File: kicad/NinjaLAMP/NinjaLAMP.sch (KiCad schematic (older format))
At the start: 33 parts, among them J1 Barrel_Jack_Switch, J2 Conn_01x05_Male, Q1 BSP89, Q2 BSP89, SW0 DIP-BUTTON_2P-6.0X3.0X4.3MM_, SW1 DIP-BUTTON_2P-6.0X3.0X4.3MM_, SW2 DIP-BUTTON_2P-6.0X3.0X4.3MM_, U1 SeeeduinoXIAO

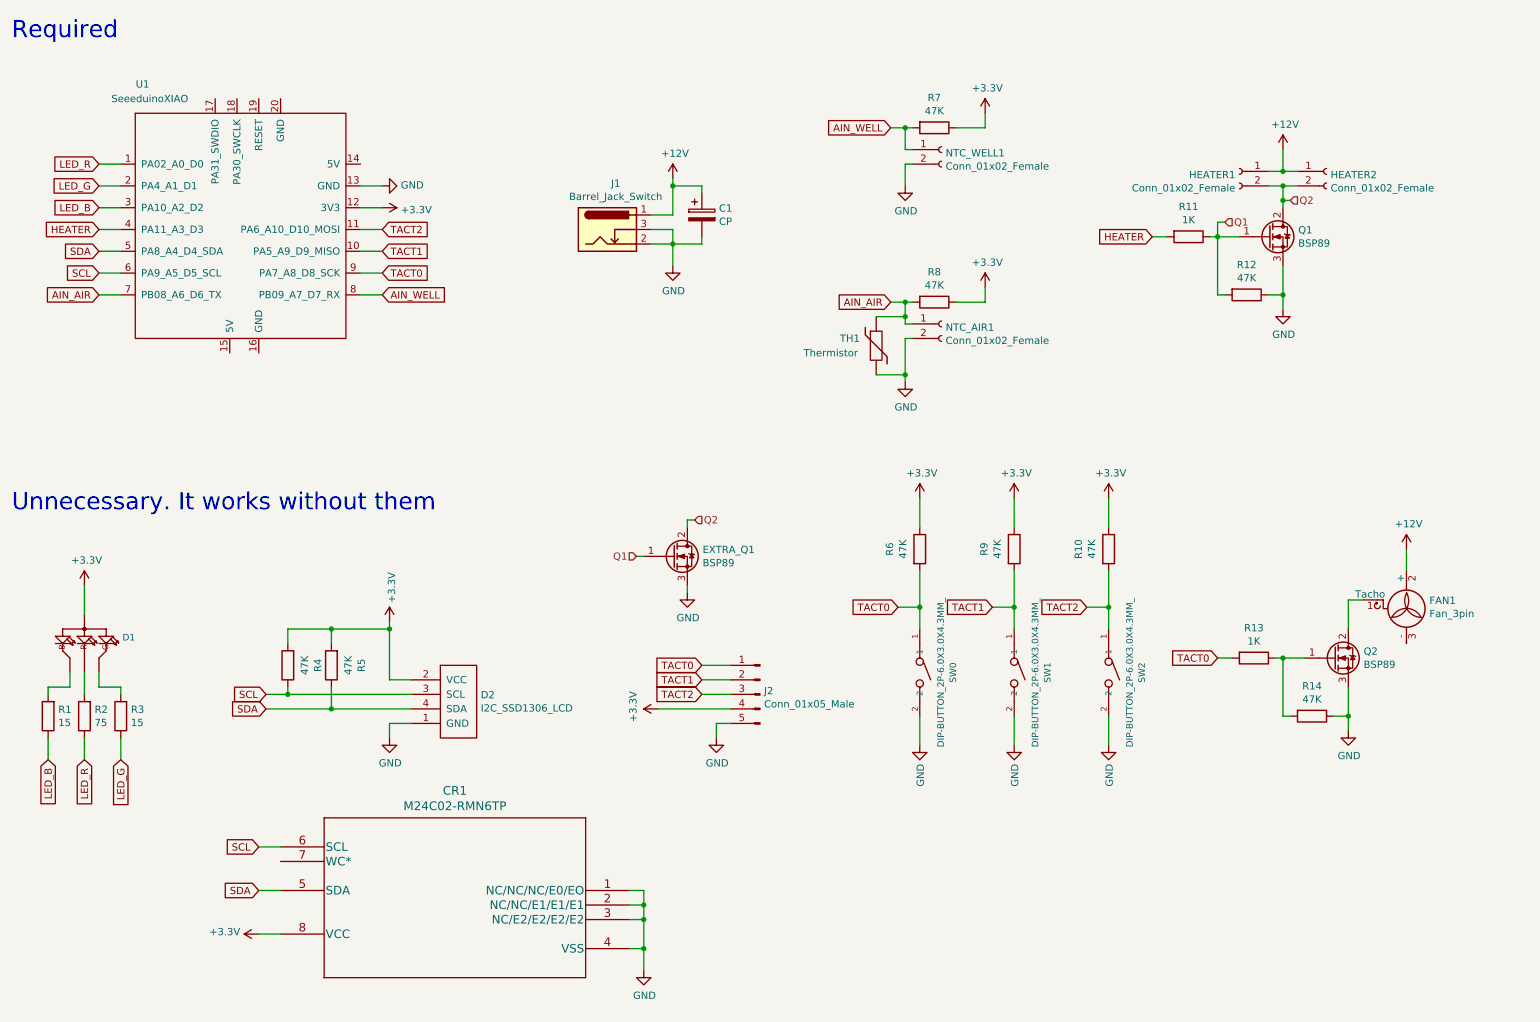
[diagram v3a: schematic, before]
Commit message: added 1x8 and 2x8 iges
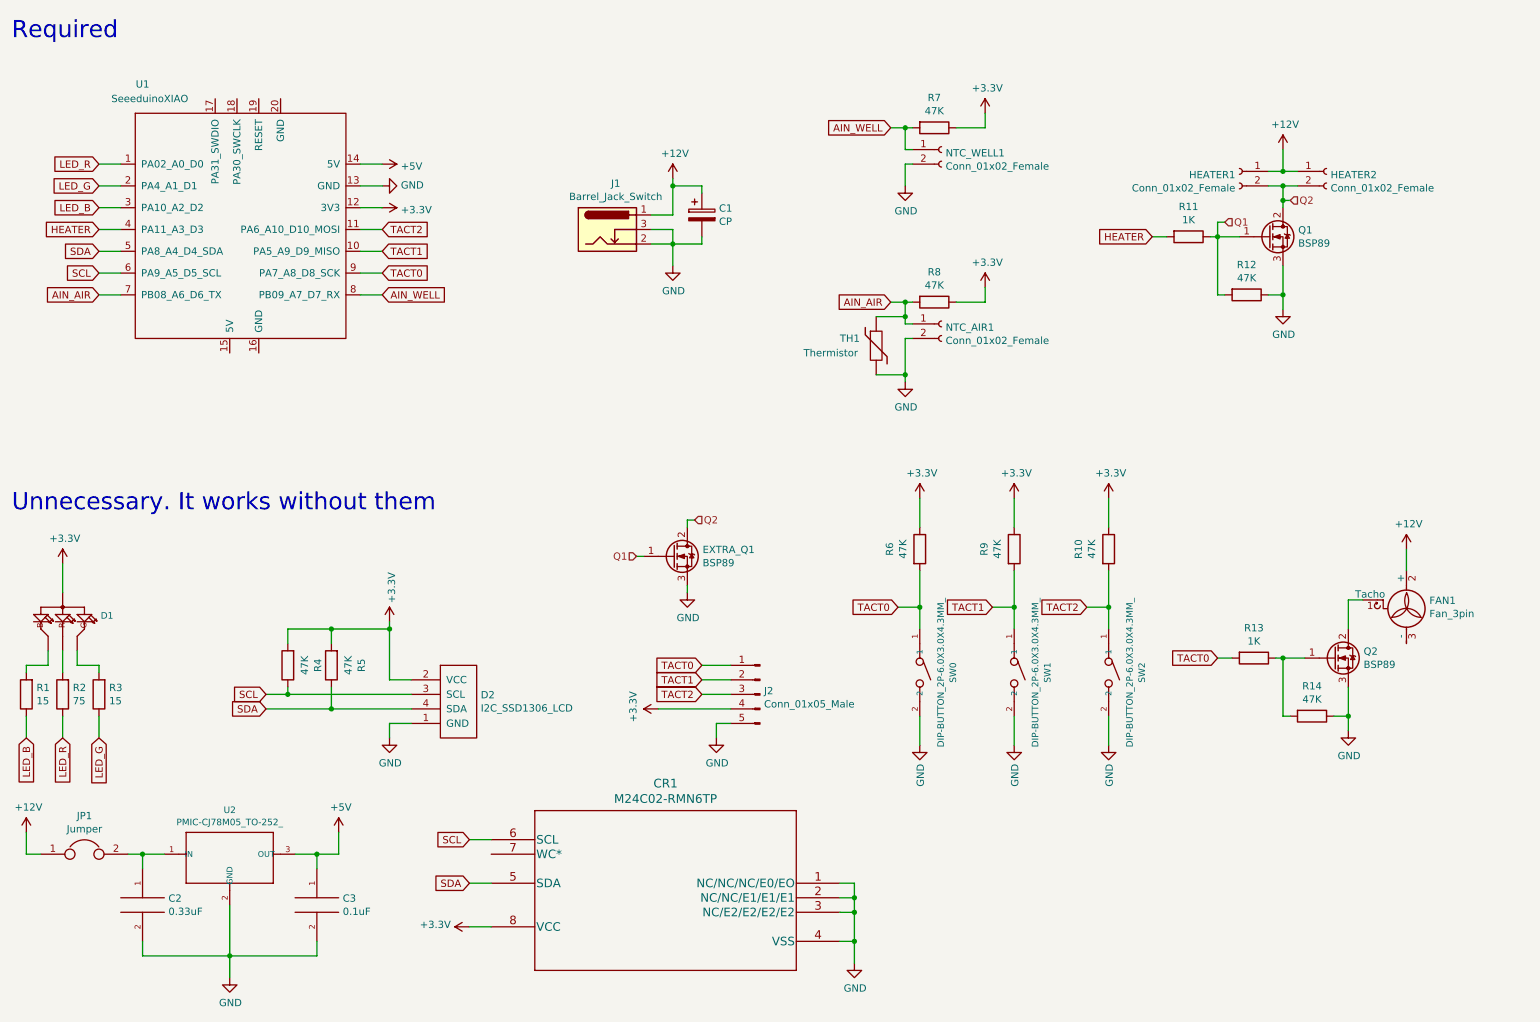
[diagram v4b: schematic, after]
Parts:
- added C2: 0.33uF, Capacitors_SMD:C_0603_HandSoldering, symbol pspice:C
- added C3: 0.1uF, Capacitors_SMD:C_0603_HandSoldering, symbol pspice:C
- added JP1: Jumper, Jumper:SolderJumper-2_P1.3mm_Open_TrianglePad1.0x1.5mm, symbol Device:Jumper
- added U2: PMIC-CJ78M05_TO-252_, OPL_Integrated_Circuit:TO-252, symbol OPL_Integrated_Circuit:PMIC-CJ78M05_TO-252_
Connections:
- net +12V: now also JP1.1
- net GND: now also C2.2, C3.2, U2.2 (GND)
- net +5V: now reaches U1.14 (5V)
- net +5V: now also C3.1, U2.3 (OUT)
- new net: C2.1, JP1.2, U2.1 (IN)
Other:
- moved on the sheet: CR1, D1, R1, R2, R3

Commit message: correct MOSFET pins
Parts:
- Q1: symbol Transistor_FET:BSP89 -> Transistor_FET:BSN20
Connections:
- net GND: now also Q1.2 (S); no longer Q1.3 (S)
- net Q2: now also Q1.3 (D); no longer Q1.2 (D)
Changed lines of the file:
@@
 $EndComp
 $Comp
-L Transistor_FET:BSP89 Q1
+L Transistor_FET:BSN20 Q1
 U 1 1 5F87013A
 P 9500 2450
